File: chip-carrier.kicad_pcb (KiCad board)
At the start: 2 copper layers, 13 x 15 mm, 9 parts, among them U1 Contact_Pad, U2 Contact_Pad, U3 Contact_Pad, U4 Contact_Pad, U5 Gate_Pad, U6 Contact_Pad, U7 Contact_Pad, U8 Contact_Pad, U9 Contact_Pad

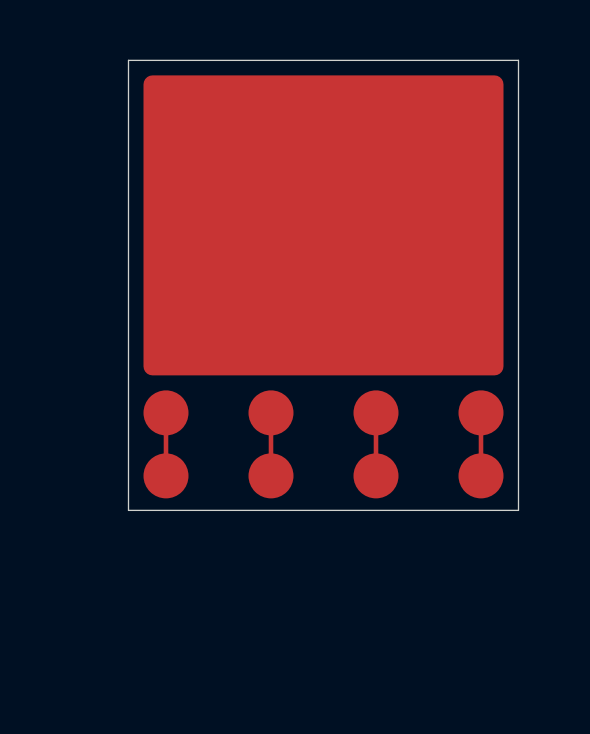
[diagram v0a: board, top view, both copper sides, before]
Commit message: Redesign contact pads
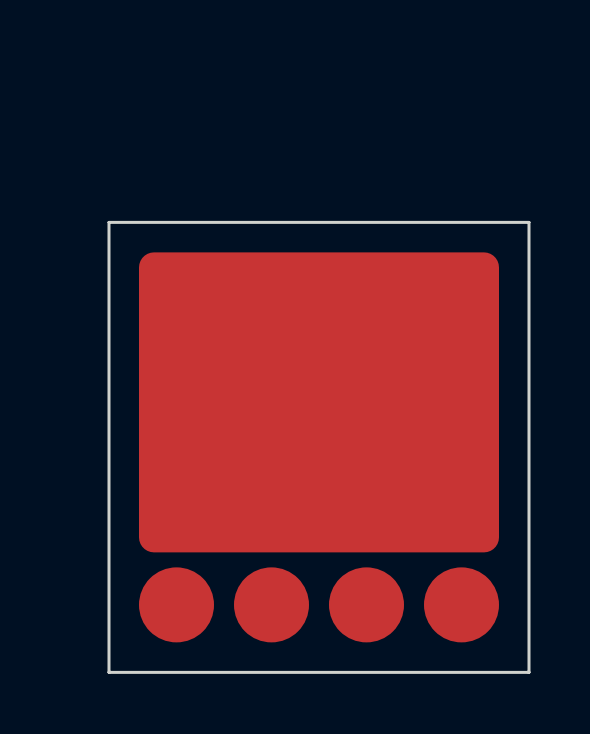
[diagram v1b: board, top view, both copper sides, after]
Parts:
- removed U6, U7, U8, U9: Contact_Pad, Chip_Carrier:C1500
- U1: value Contact_Pad -> Gate_Pad; footprint Chip_Carrier:C1500 -> chip_carrier:R12000X10000
- U2, U3, U4: footprint Chip_Carrier:C1500 -> chip_carrier:C2500
- U5: value Gate_Pad -> Contact_Pad; footprint Chip_Carrier:R12000X10000 -> chip_carrier:C2500
- moved U4 180.7 mm to (145.2, 107.2)
- moved U1 176.0 mm to (149.9, 100.2)
- moved U3 173.6 mm to (151.6, 107.2)
- moved U5 172.6 mm to (148.3, 107.2)
- moved U2 170.3 mm to (154.6, 107.1)
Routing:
- net (no net): track 8.40 -> 0.00 mm
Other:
- board size 13 x 15 mm -> 14 x 15 mm
- board text added: "CHIP CARRIER JUSTIN ZHOU EDA LAB"
- board text added: "V02"
- board text removed: "Justin Zhou Eda Lab Chip Carrier"
- board text removed: "v01"
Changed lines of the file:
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@@
   )
   (paper "A4")
+  (title_block
+    (title "Chip Carrier")
+    (date "2022-01-27")
+    (rev "v02")
+    (comment 2 "creativecommons.org/licenses/by/4.0/")
+    (comment 3 "License: CC BY 4.0")
+    (comment 4 "Author: Justin Zhou")
+  )
   (layers
     (0 "F.Cu" signal)
@@
   )
   (net 0 "")
-  (footprint "Chip_Carrier:C1500" (layer "F.Cu")
-    (at 298.15 200.2)
+  (footprint "chip_carrier:R12000X10000" (layer "F.Cu")
+    (at 149.9 100.25)
     (property "Sheetfile" "chip-carrier.kicad_sch")
     (property "Sheetname" "")
-    (fp_text reference "U3" (at -148.4 -99.4 unlocked) (layer "F.Fab")
+    (fp_text reference "U1" (at 0.1 -6.4 unlocked) (layer "F.Fab")
       (effects (font (size 1 1) (thickness 0.15)))
     )
-    (fp_text value "Contact_Pad" (at -144.85 -97.95 unlocked) (layer "F.Fab")
+    (fp_text value "Gate_Pad" (at 0 7 unlocked) (layer "F.Fab")
       (effects (font (size 1 1) (thickness 0.15)))
     )
-    (pad "3" smd circle (at -149.95 -99.45) (size 1.5 1.5) (layers "F.Cu" "F.Paste" "F.Mask"))
+    (fp_text user "${REFERENCE}" (at 0 9.8 unlocked) (layer "F.Fab")
+      (effects (font (size 1 1) (thickness 0.15)))
+    )
+    (pad "1" smd roundrect (at -0.1 0.15) (size 12 10) (layers "F.Cu" "F.Paste" "F.Mask") (roundrect_rratio 0.05))
   )
-  (footprint "Chip_Carrier:C1500" (layer "F.Cu")
-    (at 305.5 203.4)
+  (footprint "chip_carrier:C2500" (layer "F.Cu")
+    (at 148.3 107.25)
     (property "Sheetfile" "chip-carrier.kicad_sch")
     (property "Sheetname" "")
-    (fp_text reference "U9" (at 0.1 -1.65 unlocked) (layer "F.Fab")
+    (fp_text reference "U5" (at 0 -2.3 unlocked) (layer "F.Fab")
       (effects (font (size 1 1) (thickness 0.15)))
     )
-    (fp_text value "Contact_Pad" (at -144.8 -101.45 unlocked) (layer "F.Fab")
+    (fp_text value "Contact_Pad" (at 0 2.55 unlocked) (layer "F.Fab")
       (effects (font (size 1 1) (thickness 0.15)))
     )
-    (fp_text user "${REFERENCE}" (at -148.25 -100.55 unlocked) (layer "F.Fab")
+    (fp_text user "${REFERENCE}" (at 0 4.95 unlocked) (layer "F.Fab")
       (effects (font (size 1 1) (thickness 0.15)))
     )
-    (pad "9" smd circle (at -150.3 -100.55) (size 1.5 1.5) (layers "F.Cu" "F.Paste" "F.Mask"))
+    (pad "3" smd circle (at -0.083333 -0.1) (size 2.5 2.5) (layers "F.Cu" "F.Paste" "F.Mask"))
   )
-  (footprint "Chip_Carrier:C1500" (layer "F.Cu")
-    (at 301.8 200.35)
+  (footprint "chip_carrier:C2500" (layer "F.Cu")
+    (at 151.55 107.15)
     (property "Sheetfile" "chip-carrier.kicad_sch")
     (property "Sheetname" "")
-    (fp_text reference "U6" (at -148.4 -99.55 unlocked) (layer "F.Fab")
+    (fp_text reference "U3" (at 0 -2.3 unlocked) (layer "F.Fab")
       (effects (font (size 1 1) (thickness 0.15)))
     )
-    (fp_text value "Contact_Pad" (at -144.9 -98.25 unlocked) (layer "F.Fab")
+    (fp_text value "Contact_Pad" (at 0 2.55 unlocked) (layer "F.Fab")
       (effects (font (size 1 1) (thickness 0.15)))
     )
-    (pad "6" smd circle (at -150.1 -99.6) (size 1.5 1.5) (layers "F.Cu" "F.Paste" "F.Mask"))
+    (fp_text user "${REFERENCE}" (at 0 4.95 unlocked) (layer "F.Fab")
+      (effects (font (size 1 1) (thickness 0.15)))
+    )
+    (pad "4" smd circle (at -0.166667 0) (size 2.5 2.5) (layers "F.Cu" "F.Paste" "F.Mask"))
   )
-  (footprint "Chip_Carrier:C1500" (layer "F.Cu")
-    (at 304.85 200.2)
+  (footprint "chip_carrier:C2500" (layer "F.Cu")
+    (at 145.15 107.15)
     (property "Sheetfile" "chip-carrier.kicad_sch")
     (property "Sheetname" "")
-    (fp_text reference "U8" (at -147.6 -99.45 unlocked) (layer "F.Fab")
+    (fp_text reference "U4" (at 0 -2.3 unlocked) (layer "F.Fab")
       (effects (font (size 1 1) (thickness 0.15)))
     )
-    (fp_text value "Contact_Pad" (at -144.15 -95.35 unlocked) (layer "F.Fab")
+    (fp_text value "Contact_Pad" (at 0 2.55 unlocked) (layer "F.Fab")
       (effects (font (size 1 1) (thickness 0.15)))
     )
-    (pad "8" smd circle (at -149.65 -99.45) (size 1.5 1.5) (layers "F.Cu" "F.Paste" "F.Mask"))
+    (fp_text user "${REFERENCE}" (at 0 4.95 unlocked) (layer "F.Fab")
+      (effects (font (size 1 1) (thickness 0.15)))
+    )
+    (pad "2" smd circle (at -0.1 0) (size 2.5 2.5) (layers "F.Cu" "F.Paste" "F.Mask"))
   )
-  (footprint "Chip_Carrier:C1500" (layer "F.Cu")
-    (at 301.8 203.3)
+  (footprint "chip_carrier:C2500" (layer "F.Cu")
+    (at 154.6 107.1)
     (property "Sheetfile" "chip-carrier.kicad_sch")
     (property "Sheetname" "")
-    (fp_text reference "U7" (at 0.1 -1.65 unlocked) (layer "F.Fab")
+    (fp_text reference "U2" (at 0 -2.3 unlocked) (layer "F.Fab")
       (effects (font (size 1 1) (thickness 0.15)))
     )
-    (fp_text value "Contact_Pad" (at -151.95 -98.65 unlocked) (layer "F.Fab")
+    (fp_text value "Contact_Pad" (at 0 2.55 unlocked) (layer "F.Fab")
       (effects (font (size 1 1) (thickness 0.15)))
     )
-    (fp_text user "${REFERENCE}" (at -148.45 -100.4 unlocked) (layer "F.Fab")
+    (fp_text user "${REFERENCE}" (at 0 4.95 unlocked) (layer "F.Fab")
       (effects (font (size 1 1) (thickness 0.15)))
     )
-    (pad "7" smd circle (at -150.1 -100.45) (size 1.5 1.5) (layers "F.Cu" "F.Paste" "F.Mask"))
+    (pad "5" smd circle (at -0.05 0.05) (size 2.5 2.5) (layers "F.Cu" "F.Paste" "F.Mask"))
   )
-  (footprint "Chip_Carrier:C1500" (layer "F.Cu")
-    (at 294.85 200.15)
-    (property "Sheetfile" "chip-carrier.kicad_sch")
-    (property "Sheetname" "")
-    (fp_text reference "U1" (at -148.6 -99.3 unlocked) (layer "F.Fab")
-      (effects (font (size 1 1) (thickness 0.15)))
-    )
-    (fp_text value "Contact_Pad" (at -138 -95.65 unlocked) (layer "F.Fab")
-      (effects (font (size 1 1) (thickness 0.15)))
-    )
-    (pad "1" smd circle (at -150.15 -99.4) (size 1.5 1.5) (layers "F.Cu" "F.Paste" "F.Mask"))
+  (gr_line (start 142.8 94.4) (end 156.8 94.4) (layer "Edge.Cuts") (width 0.1))
+  (gr_line (start 142.8 109.4) (end 142.8 94.4) (layer "Edge.Cuts") (width 0.1))
+  (gr_line (start 156.8 109.4) (end 142.8 109.4) (layer "Edge.Cuts") (width 0.1))
+  (gr_line (start 156.8 94.4) (end 156.8 109.4) (layer "Edge.Cuts") (width 0.1))
+  (gr_text "V02" (at 144.6 99.55 -90) (layer "B.Cu")
+    (effects (font (size 1.5 1.5) (thickness 0.3)) (justify left mirror))
   )
-  (footprint "Chip_Carrier:C1500" (layer "F.Cu")
-    (at 298.05 203.4)
-    (property "Sheetfile" "chip-carrier.kicad_sch")
-    (property "Sheetname" "")
-    (fp_text reference "U4" (at 0.1 -1.65 unlocked) (layer "F.Fab")
-      (effects (font (size 1 1) (thickness 0.15)))
-    )
-    (fp_text value "Contact_Pad" (at -148.15 -101.2 unlocked) (layer "F.Fab")
-      (effects (font (size 1 1) (thickness 0.15)))
-    )
-    (fp_text user "${REFERENCE}" (at -148.3 -100.5 unlocked) (layer "F.Fab")
-      (effects (font (size 1 1) (thickness 0.15)))
-    )
-    (pad "4" smd circle (at -149.85 -100.55) (size 1.5 1.5) (layers "F.Cu" "F.Paste" "F.Mask"))
+  (gr_text "CHIP CARRIER\nJUSTIN ZHOU\nEDA LAB" (at 153.6 108.7 -90) (layer "B.SilkS")
+    (effects (font (size 1 1) (thickness 0.15)) (justify left mirror))
   )
-  (footprint "Chip_Carrier:R12000X10000" (layer "F.Cu")
-    (at 300.05 189.55)
-    (property "Sheetfile" "chip-carrier.kicad_sch")
-    (property "Sheetname" "")
-    (fp_text reference "U5" (at -143.3 -99.15 unlocked) (layer "F.Fab")
-      (effects (font (size 1 1) (thickness 0.15)))
-    )
-    (fp_text value "Gate_Pad" (at -139.85 -90.9 unlocked) (layer "F.Fab")
-      (effects (font (size 1 1) (thickness 0.15)))
-    )
-    (pad "5" smd roundrect (at -150.1 -95.05) (size 12 10) (layers "F.Cu" "F.Paste" "F.Mask") (roundrect_rratio 0.03))
-  )
-  (footprint "Chip_Carrier:C1500" (layer "F.Cu")
-    (at 294.9 203.55)
-    (property "Sheetfile" "chip-carrier.kicad_sch")
-    (property "Sheetname" "")
-    (fp_text reference "U2" (at 0.1 -1.65 unlocked) (layer "F.Fab")
-      (effects (font (size 1 1) (thickness 0.15)))
-    )
-    (fp_text value "Contact_Pad" (at -141.45 -98.85 unlocked) (layer "F.Fab")
-      (effects (font (size 1 1) (thickness 0.15)))
-    )
-    (fp_text user "${REFERENCE}" (at -148.6 -100.65 unlocked) (layer "F.Fab")
-      (effects (font (size 1 1) (thickness 0.15)))
-    )
-    (pad "2" smd circle (at -150.2 -100.7) (size 1.5 1.5) (layers "F.Cu" "F.Paste" "F.Mask"))
-  )
-  (gr_line (start 156.45 104) (end 156.45 89) (layer "Edge.Cuts") (width 0.0254))
-  (gr_line (start 143.45 104) (end 156.45 104) (layer "Edge.Cuts") (width 0.0254))
-  (gr_line (start 143.45 104) (end 143.45 89) (layer "Edge.Cuts") (width 0.0254))
-  (gr_line (start 143.45 89) (end 156.45 89) (layer "Edge.Cuts") (width 0.0254))
-  (gr_text "v01" (at 144.7 90.9 -90) (layer "B.Cu")
-    (effects (font (size 1 1) (thickness 0.1)) (justify mirror))
-  )
-  (gr_text "Justin Zhou\nEda Lab\nChip Carrier" (at 153.5 103.25 -90) (layer "B.SilkS")
-    (effects (font (size 1 1) (thickness 0.1)) (justify left mirror))
-  )
-  (segment (start 144.7 100.75) (end 144.7 102.85) (width 0.1524) (layer "F.Cu") (net 0))
-  (segment (start 151.7 100.75) (end 151.7 102.85) (width 0.1524) (layer "F.Cu") (net 0))
-  (segment (start 155.2 100.75) (end 155.2 102.85) (width 0.1524) (layer "F.Cu") (net 0))
-  (segment (start 148.2 100.75) (end 148.2 102.85) (width 0.1524) (layer "F.Cu") (net 0))
 )

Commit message: Change contact pads to rounded rectangular shape
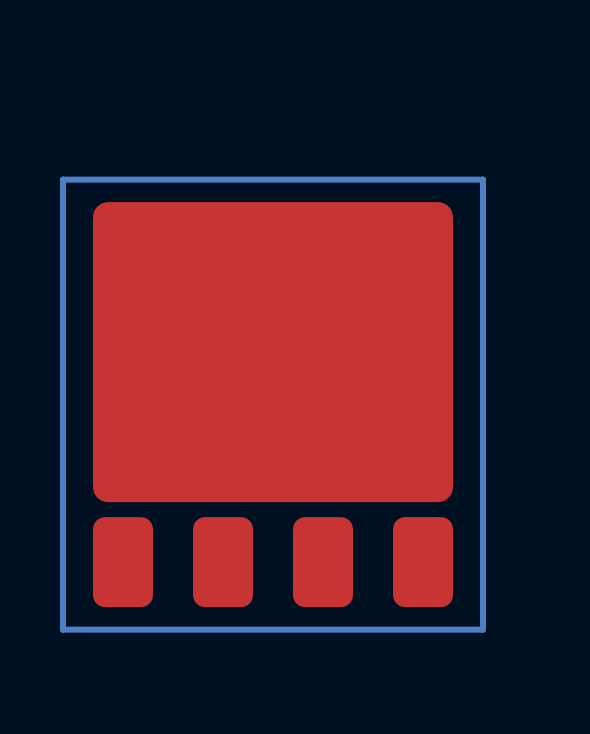
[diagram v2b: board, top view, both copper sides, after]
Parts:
- U2, U3, U4, U5: footprint chip_carrier:C2500 -> chip_carrier:R2000X3000
- moved U1 178.5 mm to (293.9, 205.7)
- moved U4 4.93 mm to (143.3, 111.7)
- moved U3 4.92 mm to (149.9, 111.8)
- moved U2 4.89 mm to (153.0, 111.7)
- moved U5 4.73 mm to (146.8, 111.7)
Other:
- board outline removed
- board text added: "Chip carrier Justin Zhou Eda Lab"
- board text added: "v03"
- board text removed: "CHIP CARRIER JUSTIN ZHOU EDA LAB"
- board text removed: "V02"
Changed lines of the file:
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@@
   (title_block
     (title "Chip Carrier")
-    (date "2022-01-27")
-    (rev "v02")
+    (date "2022-02-08")
+    (rev "v03")
     (comment 2 "creativecommons.org/licenses/by/4.0/")
     (comment 3 "License: CC BY 4.0")
@@
   )
   (net 0 "")
+  (footprint "chip_carrier:R2000X3000" (layer "F.Cu")
+    (at 146.766667 111.725)
+    (property "Sheetfile" "chip-carrier.kicad_sch")
+    (property "Sheetname" "")
+    (fp_text reference "U5" (at 0.1 -6.4 unlocked) (layer "F.Fab")
+      (effects (font (size 1 1) (thickness 0.15)))
+    )
+    (fp_text value "Contact_Pad" (at 0 7 unlocked) (layer "F.Fab")
+      (effects (font (size 1 1) (thickness 0.15)))
+    )
+    (fp_text user "${REFERENCE}" (at 0 9.8 unlocked) (layer "F.Fab")
+      (effects (font (size 1 1) (thickness 0.15)))
+    )
+    (pad "3" smd roundrect (at -0.166667 -6) (size 2 3) (layers "F.Cu" "F.Paste" "F.Mask") (roundrect_rratio 0.2))
+  )
+  (footprint "chip_carrier:R2000X3000" (layer "F.Cu")
+    (at 143.316667 111.725)
+    (property "Sheetfile" "chip-carrier.kicad_sch")
+    (property "Sheetname" "")
+    (fp_text reference "U4" (at 0.1 -6.4 unlocked) (layer "F.Fab")
+      (effects (font (size 1 1) (thickness 0.15)))
+    )
+    (fp_text value "Contact_Pad" (at 0 7 unlocked) (layer "F.Fab")
+      (effects (font (size 1 1) (thickness 0.15)))
+    )
+    (fp_text user "${REFERENCE}" (at 0 9.8 unlocked) (layer "F.Fab")
+      (effects (font (size 1 1) (thickness 0.15)))
+    )
+    (pad "2" smd roundrect (at -0.05 -6) (size 2 3) (layers "F.Cu" "F.Paste" "F.Mask") (roundrect_rratio 0.2))
+  )
+  (footprint "chip_carrier:R2000X3000" (layer "F.Cu")
+    (at 153.016667 111.725)
+    (property "Sheetfile" "chip-carrier.kicad_sch")
+    (property "Sheetname" "")
+    (fp_text reference "U2" (at 0.1 -6.4 unlocked) (layer "F.Fab")
+      (effects (font (size 1 1) (thickness 0.15)))
+    )
+    (fp_text value "Contact_Pad" (at 0 7 unlocked) (layer "F.Fab")
+      (effects (font (size 1 1) (thickness 0.15)))
+    )
+    (fp_text user "${REFERENCE}" (at 0 9.8 unlocked) (layer "F.Fab")
+      (effects (font (size 1 1) (thickness 0.15)))
+    )
+    (pad "5" smd roundrect (at 0.25 -6) (size 2 3) (layers "F.Cu" "F.Paste" "F.Mask") (roundrect_rratio 0.2))
+  )
   (footprint "chip_carrier:R12000X10000" (layer "F.Cu")
-    (at 149.9 100.25)
+    (at 293.916667 205.725)
     (property "Sheetfile" "chip-carrier.kicad_sch")
     (property "Sheetname" "")
@@
       (effects (font (size 1 1) (thickness 0.15)))
     )
-    (pad "1" smd roundrect (at -0.1 0.15) (size 12 10) (layers "F.Cu" "F.Paste" "F.Mask") (roundrect_rratio 0.05))
+    (pad "1" smd roundrect (at -145.65 -107) (size 12 10) (layers "F.Cu" "F.Paste" "F.Mask") (roundrect_rratio 0.05))
   )
-  (footprint "chip_carrier:C2500" (layer "F.Cu")
-    (at 148.3 107.25)
+  (footprint "chip_carrier:R2000X3000" (layer "F.Cu")
+    (at 149.866667 111.775)
     (property "Sheetfile" "chip-carrier.kicad_sch")
     (property "Sheetname" "")
-    (fp_text reference "U5" (at 0 -2.3 unlocked) (layer "F.Fab")
+    (fp_text reference "U3" (at 0.1 -6.4 unlocked) (layer "F.Fab")
       (effects (font (size 1 1) (thickness 0.15)))
     )
-    (fp_text value "Contact_Pad" (at 0 2.55 unlocked) (layer "F.Fab")
+    (fp_text value "Contact_Pad" (at 0 7 unlocked) (layer "F.Fab")
       (effects (font (size 1 1) (thickness 0.15)))
     )
-    (fp_text user "${REFERENCE}" (at 0 4.95 unlocked) (layer "F.Fab")
+    (fp_text user "${REFERENCE}" (at 0 9.8 unlocked) (layer "F.Fab")
       (effects (font (size 1 1) (thickness 0.15)))
     )
-    (pad "3" smd circle (at -0.083333 -0.1) (size 2.5 2.5) (layers "F.Cu" "F.Paste" "F.Mask"))
+    (pad "4" smd roundrect (at 0.066667 -6.05) (size 2 3) (layers "F.Cu" "F.Paste" "F.Mask") (roundrect_rratio 0.2))
   )
-  (footprint "chip_carrier:C2500" (layer "F.Cu")
-    (at 151.55 107.15)
-    (property "Sheetfile" "chip-carrier.kicad_sch")
-    (property "Sheetname" "")
-    (fp_text reference "U3" (at 0 -2.3 unlocked) (layer "F.Fab")
-      (effects (font (size 1 1) (thickness 0.15)))
-    )
-    (fp_text value "Contact_Pad" (at 0 2.55 unlocked) (layer "F.Fab")
-      (effects (font (size 1 1) (thickness 0.15)))
-    )
-    (fp_text user "${REFERENCE}" (at 0 4.95 unlocked) (layer "F.Fab")
-      (effects (font (size 1 1) (thickness 0.15)))
-    )
-    (pad "4" smd circle (at -0.166667 0) (size 2.5 2.5) (layers "F.Cu" "F.Paste" "F.Mask"))
-  )
-  (footprint "chip_carrier:C2500" (layer "F.Cu")
-    (at 145.15 107.15)
-    (property "Sheetfile" "chip-carrier.kicad_sch")
-    (property "Sheetname" "")
-    (fp_text reference "U4" (at 0 -2.3 unlocked) (layer "F.Fab")
-      (effects (font (size 1 1) (thickness 0.15)))
-    )
-    (fp_text value "Contact_Pad" (at 0 2.55 unlocked) (layer "F.Fab")
-      (effects (font (size 1 1) (thickness 0.15)))
-    )
-    (fp_text user "${REFERENCE}" (at 0 4.95 unlocked) (layer "F.Fab")
-      (effects (font (size 1 1) (thickness 0.15)))
-    )
-    (pad "2" smd circle (at -0.1 0) (size 2.5 2.5) (layers "F.Cu" "F.Paste" "F.Mask"))
-  )
-  (footprint "chip_carrier:C2500" (layer "F.Cu")
-    (at 154.6 107.1)
-    (property "Sheetfile" "chip-carrier.kicad_sch")
-    (property "Sheetname" "")
-    (fp_text reference "U2" (at 0 -2.3 unlocked) (layer "F.Fab")
-      (effects (font (size 1 1) (thickness 0.15)))
-    )
-    (fp_text value "Contact_Pad" (at 0 2.55 unlocked) (layer "F.Fab")
-      (effects (font (size 1 1) (thickness 0.15)))
-    )
-    (fp_text user "${REFERENCE}" (at 0 4.95 unlocked) (layer "F.Fab")
-      (effects (font (size 1 1) (thickness 0.15)))
-    )
-    (pad "5" smd circle (at -0.05 0.05) (size 2.5 2.5) (layers "F.Cu" "F.Paste" "F.Mask"))
-  )
-  (gr_line (start 142.8 94.4) (end 156.8 94.4) (layer "Edge.Cuts") (width 0.1))
-  (gr_line (start 142.8 109.4) (end 142.8 94.4) (layer "Edge.Cuts") (width 0.1))
-  (gr_line (start 156.8 109.4) (end 142.8 109.4) (layer "Edge.Cuts") (width 0.1))
-  (gr_line (start 156.8 94.4) (end 156.8 109.4) (layer "Edge.Cuts") (width 0.1))
-  (gr_text "V02" (at 144.6 99.55 -90) (layer "B.Cu")
+  (gr_line (start 141.266667 92.975) (end 141.266667 107.975) (layer "B.Cu") (width 0.2))
+  (gr_line (start 141.266667 92.975) (end 155.266667 92.975) (layer "B.Cu") (width 0.2))
+  (gr_line (start 155.266667 107.975) (end 141.266667 107.975) (layer "B.Cu") (width 0.2))
+  (gr_line (start 155.266667 107.975) (end 155.266667 92.975) (layer "B.Cu") (width 0.2))
+  (gr_text "v03" (at 143.116667 97.725 -90) (layer "B.Cu")
     (effects (font (size 1.5 1.5) (thickness 0.3)) (justify left mirror))
   )
-  (gr_text "CHIP CARRIER\nJUSTIN ZHOU\nEDA LAB" (at 153.6 108.7 -90) (layer "B.SilkS")
+  (gr_text "Chip carrier\nJustin Zhou\nEda Lab" (at 152.116667 107.425 -90) (layer "B.SilkS")
     (effects (font (size 1 1) (thickness 0.15)) (justify left mirror))
   )

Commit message: Fix missing Edge.Cut layer
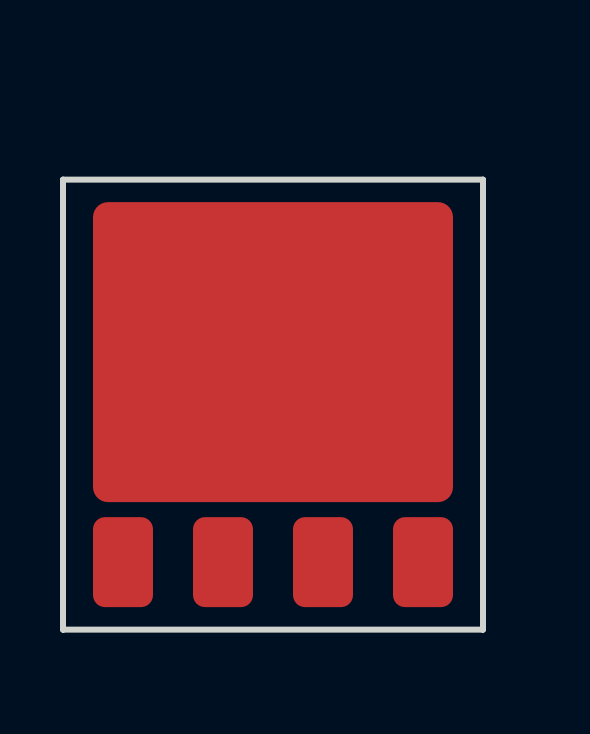
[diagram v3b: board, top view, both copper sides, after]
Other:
- board outline added: 14 x 15 mm
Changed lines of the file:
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@@
     (pad "4" smd roundrect (at 0.066667 -6.05) (size 2 3) (layers "F.Cu" "F.Paste" "F.Mask") (roundrect_rratio 0.2))
   )
-  (gr_line (start 141.266667 92.975) (end 141.266667 107.975) (layer "B.Cu") (width 0.2))
-  (gr_line (start 141.266667 92.975) (end 155.266667 92.975) (layer "B.Cu") (width 0.2))
-  (gr_line (start 155.266667 107.975) (end 141.266667 107.975) (layer "B.Cu") (width 0.2))
-  (gr_line (start 155.266667 107.975) (end 155.266667 92.975) (layer "B.Cu") (width 0.2))
+  (gr_line (start 141.266667 92.975) (end 141.266667 107.975) (layer "Edge.Cuts") (width 0.2))
+  (gr_line (start 141.266667 92.975) (end 155.266667 92.975) (layer "Edge.Cuts") (width 0.2))
+  (gr_line (start 155.266667 107.975) (end 141.266667 107.975) (layer "Edge.Cuts") (width 0.2))
+  (gr_line (start 155.266667 107.975) (end 155.266667 92.975) (layer "Edge.Cuts") (width 0.2))
   (gr_text "v03" (at 143.116667 97.725 -90) (layer "B.Cu")
     (effects (font (size 1.5 1.5) (thickness 0.3)) (justify left mirror))
